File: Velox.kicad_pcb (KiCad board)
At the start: 2 copper layers, 64 x 32.5 mm, 4 parts

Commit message: Polished design
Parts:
- added C1: C, Capacitor_SMD:C_0805_2012Metric_Pad1.18x1.45mm_HandSolder, B.Cu at (204.0, 120.8)
- added C2: C, Capacitor_SMD:C_0805_2012Metric_Pad1.18x1.45mm_HandSolder, B.Cu at (197.5, 120.8)
- added I1: L, Inductor_SMD:L_0805_2012Metric_Pad1.15x1.40mm_HandSolder, B.Cu at (200.8, 121.8)
- moved LoRa-RA-01 7.00 mm to (187.0, 114.0), turned to 90 degrees
- moved SMA1 5.35 mm to (210.2, 120.0), turned to 180 degrees
- renumbered LoRa to LoRa-RA-01, OLED to OLED1, SMA to SMA1
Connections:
- LoRa-RA-01 pad 6: unconnected-(U2-DIO1-Pad6) -> D3
- SMA1 pad 1: ANT -> Net-(SMA1-In)
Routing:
- net D3: track 0.00 -> 46.1 mm, vias 0 -> 1
- net ANT: track 40.9 -> 5.33 mm
- net D2: track 36.0 -> 47.4 mm
- net VCC_3.3: track 36.2 -> 26.7 mm
- net Net-(SMA1-In): track 0.00 -> 8.69 mm
- net MOSI: track 14.3 -> 22.6 mm
- net D1: track 40.9 -> 49.1 mm
- net MISO: track 13.5 -> 21.2 mm
- net SCK: track 12.9 -> 20.6 mm
- net D0: track 35.2 -> 30.2 mm
- net VCC_5V: track 64.7 -> 67.9 mm
- net GND: track 2.41 -> 5.19 mm, vias 1 -> 0
- net SDA: track 27.3 -> 28.2 mm
- net SCL: track 28.0 -> 28.8 mm
- added copper zone on F.Cu, net GND
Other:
- board text added: "Aaron Danton (agrd2) Adam Kerbel (alk62)"
- board text added: "Velox"

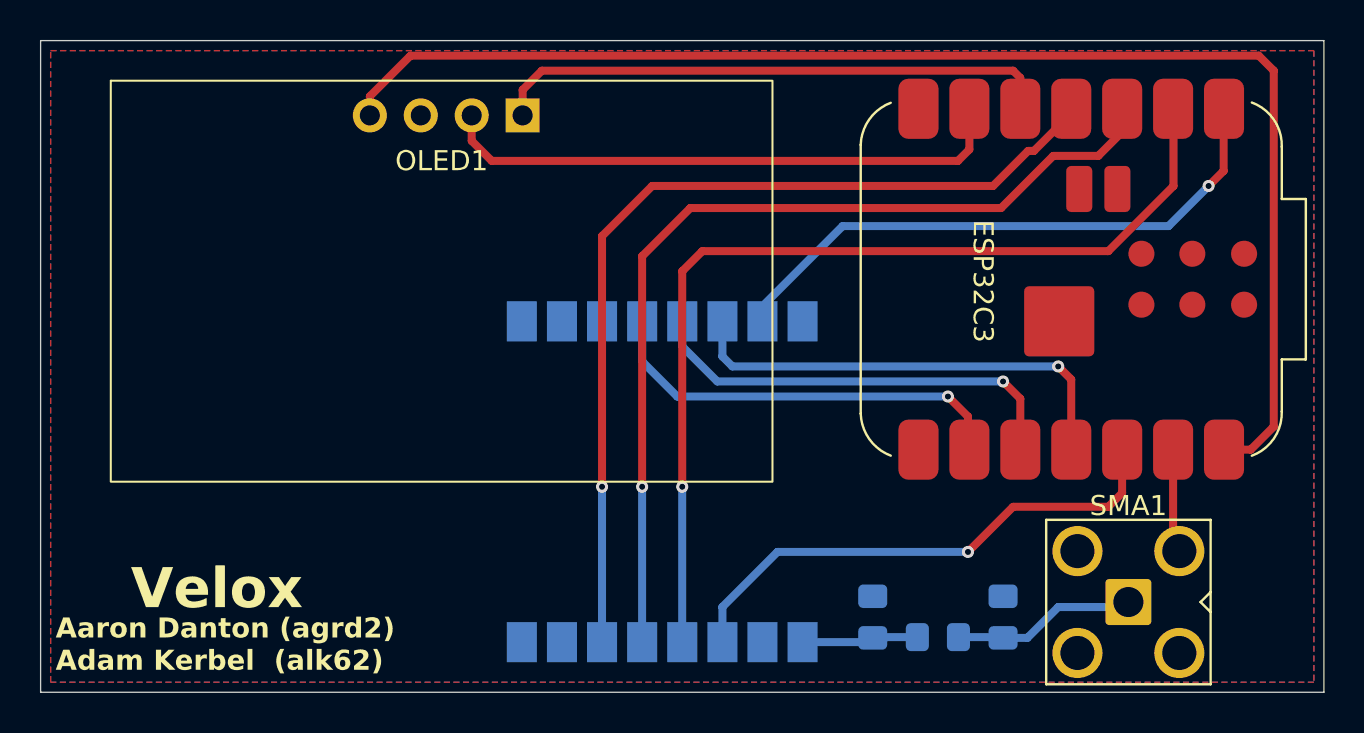
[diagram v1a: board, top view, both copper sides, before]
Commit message: Updated the PCB to feature return vias and some mounting points.
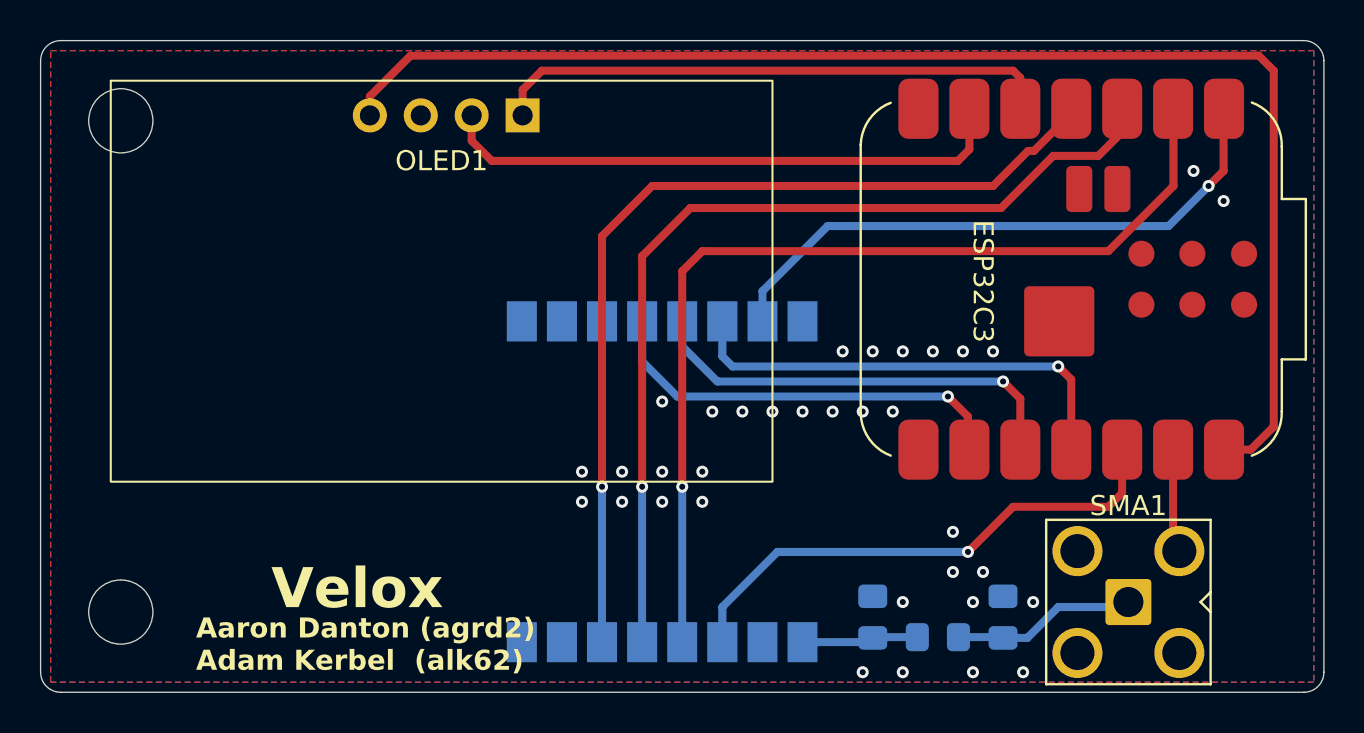
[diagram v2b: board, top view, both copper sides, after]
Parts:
- added REF**: MountingHole_3.2mm_M3, MountingHole:MountingHole_3.2mm_M3, F.Cu at (160.0, 96.0)
- added REF**: MountingHole_3.2mm_M3, MountingHole:MountingHole_3.2mm_M3, F.Cu at (160.0, 120.5)
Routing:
- net GND: vias 0 -> 34
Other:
- outline, holes or cut-outs redrawn
